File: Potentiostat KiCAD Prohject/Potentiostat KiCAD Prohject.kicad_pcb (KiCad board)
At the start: 2 copper layers, 94 x 55.9 mm, 35 parts, among them J1 USB_B_Micro, K1 DIPxx-1Axx-12xD, U1 OPA2277, U10 ADS1115IDGS, U11 MCP4725xxx-xCH, U12 RT9080-33GJ5, U2 TL074, U3 ESP32-S2, U4 OPA2277, U5 INA128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

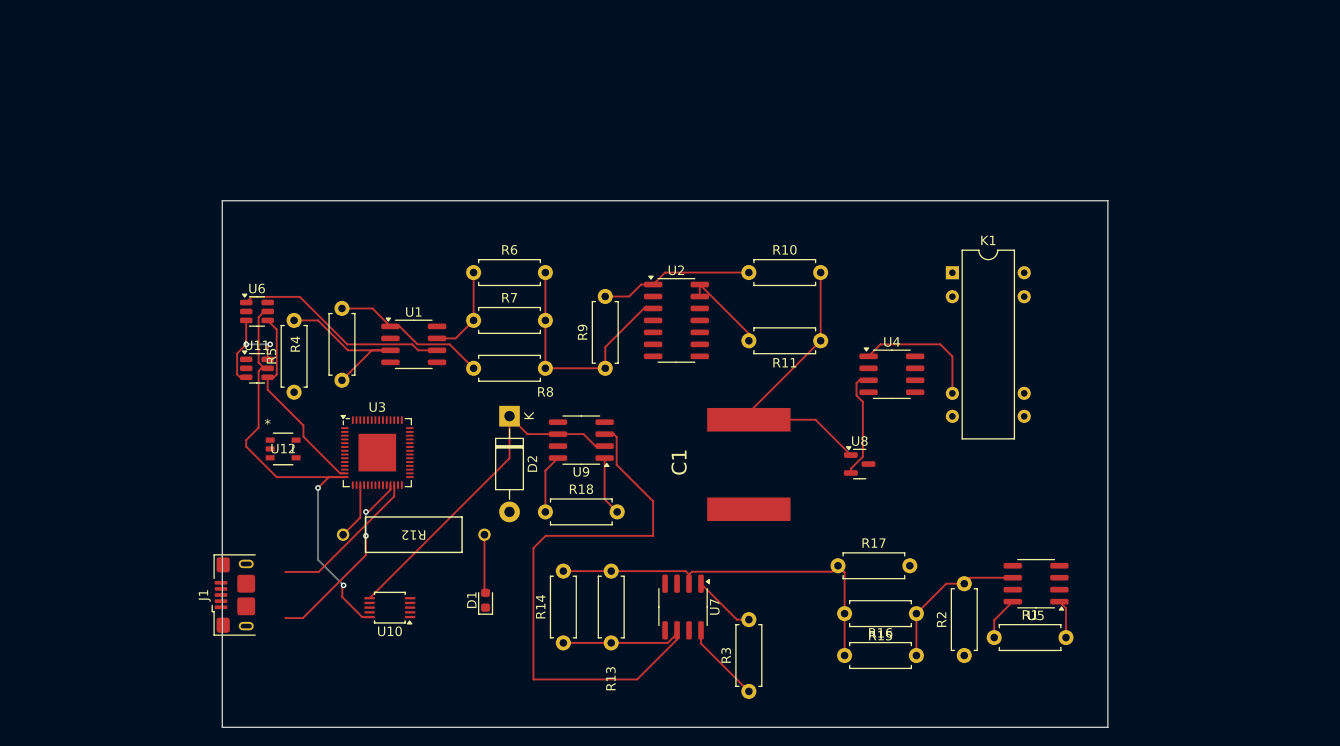
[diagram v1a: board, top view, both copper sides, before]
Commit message: Redid layout with ground traces
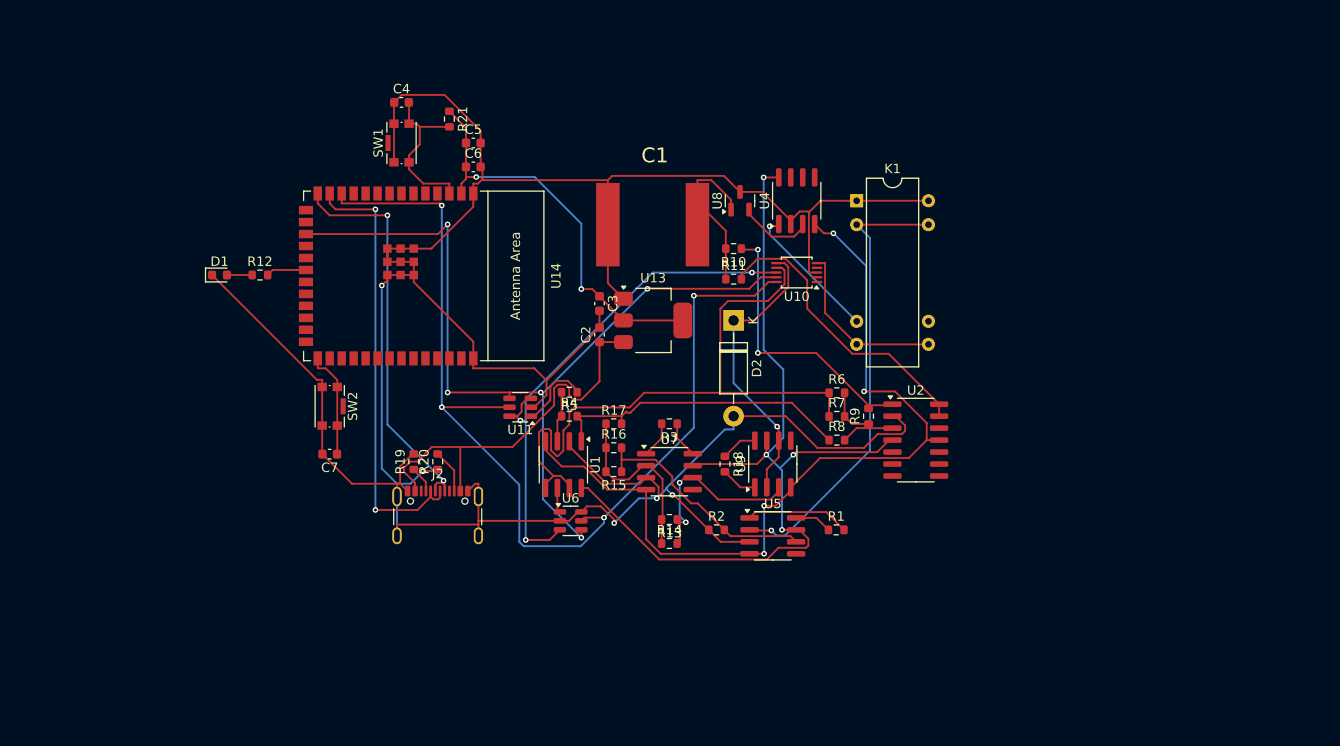
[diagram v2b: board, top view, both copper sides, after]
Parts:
- removed J1: USB_B_Micro, Connector_USB:USB_Micro-B_Amphenol_10118193-0001LF_Horizontal
- removed U12: RT9080-33GJ5, footprints:TSOT-23-5_RIT
- removed U3: ESP32-S2, Package_DFN_QFN:QFN-56-1EP_7x7mm_P0.4mm_EP4x4mm
- added C2: 100nF, Capacitor_SMD:C_0603_1608Metric, F.Cu at (172.1, 82.8)
- added C3: 10uF, Capacitor_SMD:C_0603_1608Metric, F.Cu at (172.1, 79.5)
- added C4: .1uF, Capacitor_SMD:C_0603_1608Metric, F.Cu at (151.1, 58.1)
- added C5: 1uF, Capacitor_SMD:C_0603_1608Metric, F.Cu at (158.7, 62.5)
- added C6: .1uF, Capacitor_SMD:C_0603_1608Metric, F.Cu at (158.7, 65.0)
- added C7: .1uF, Capacitor_SMD:C_0603_1608Metric, F.Cu at (143.5, 95.5)
- added J2: USB_C_Receptacle_USB2.0, Connector_USB:USB_C_Receptacle_GCT_USB4105-xx-A_16P_TopMnt_Horizontal, F.Cu at (154.9, 103.1)
- added R19: 5.1 k, Resistor_SMD:R_0603_1608Metric, F.Cu at (152.4, 96.3)
- added R20: 5.1 k, Resistor_SMD:R_0603_1608Metric, F.Cu at (154.9, 96.3)
- added R21: 10k, Resistor_SMD:R_0603_1608Metric, F.Cu at (156.2, 59.9)
- added SW1: Reset, Button_Switch_SMD:SW_Push_1P1T-SH_NO_CK_KMR2xxG, F.Cu at (151.1, 62.5)
- added SW2: Boot, Button_Switch_SMD:SW_Push_1P1T-SH_NO_CK_KMR2xxG, F.Cu at (143.5, 90.4)
- added U13: LD1117S33TR_SOT223, Package_TO_SOT_SMD:SOT-223-3_TabPin2, F.Cu at (177.8, 81.3)
- added U14: ESP32-S2-SOLO, ESP32:ESP32-S2-SOLO, F.Cu at (150.5, 76.6)
- R1, R10, R11, R13, R14, R15, R16, R17, R18, R2, R3, R4, R5, R6, R7, R8, R9: footprint Resistor_THT:R_Axial_DIN0207_L6.3mm_D2.5mm_P7.62mm_Horizontal -> Resistor_SMD:R_0603_1608Metric
- R12: footprint footprints:res2_1-1625885-7_TEC -> Resistor_SMD:R_0603_1608Metric
- moved U10 55.9 mm to (193.0, 76.2)
- moved D1 44.6 mm to (131.8, 76.5), turned to 0 degrees
- moved R6 40.6 mm to (197.3, 89.0)
- moved U6 40.0 mm to (169.0, 102.5)
- moved R7 39.9 mm to (197.3, 91.5)
- moved R8 39.3 mm to (197.3, 94.0)
- moved R12 36.4 mm to (136.1, 76.5), turned to 0 degrees
- moved R15 35.5 mm to (173.6, 97.3)
- moved R16 33.0 mm to (173.6, 94.8)
- moved U8 30.7 mm to (187.0, 68.6), turned to 90 degrees
- moved R3 29.6 mm to (179.5, 92.2), turned to 180 degrees
- moved R2 29.5 mm to (184.5, 103.5), turned to 0 degrees
- moved R5 29.2 mm to (168.9, 88.9), turned to 180 degrees
- moved U2 28.4 mm to (205.7, 94.0)
- moved R9 28.4 mm to (200.7, 91.4)
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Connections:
- net Net-(U10-AIN3) renamed /ADC_IN3
- net Net-(U10-SCL) renamed /I2C_SCL
- net Net-(U10-SDA) renamed /I2C_SDA
- R14 pad 1: Net-(U9-+) -> Net-(U7--)
- R14 pad 2: Net-(U7--) -> Net-(U9-+)
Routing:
- net GND: track 0.00 -> 323.6 mm, vias 0 -> 5
- net +9V: track 0.00 -> 96.0 mm, vias 0 -> 4
- net -9V: track 0.00 -> 89.1 mm, vias 0 -> 4
- net /I2C_SDA: track 21.1 -> 91.8 mm, vias 0 -> 5
- net /I2C_SCL: track 48.5 -> 108.2 mm, vias 2 -> 4
- net /ADC_IN3: track 9.74 -> 69.2 mm
- net Net-(U9-+): track 71.5 -> 20.4 mm, vias 0 -> 2
- net /Working Electrode: track 0.00 -> 48.9 mm, vias 0 -> 1
- net /D-: track 0.00 -> 47.0 mm, vias 0 -> 2
- net VCC: track 11.5 -> 55.9 mm, vias 2 -> 3
- net +3.3V: track 0.00 -> 43.0 mm, vias 0 -> 2
- net /D+: track 0.00 -> 42.4 mm, vias 0 -> 2
- net +5V: track 0.00 -> 41.7 mm
- net Net-(U2D--): track 9.40 -> 31.6 mm
- net Net-(U7--): track 40.5 -> 19.5 mm
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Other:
- board outline removed

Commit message: we're so back
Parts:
- added J1: Conn_01x02_Pin, Connector_PinHeader_2.54mm:PinHeader_1x02_P2.54mm_Vertical, F.Cu at (190.5, 61.0)
- added J3: Conn_01x02_Pin, Connector_PinHeader_2.54mm:PinHeader_1x02_P2.54mm_Vertical, F.Cu at (195.6, 58.4)
- added J4: Reference, i made this:CONN_575-8_KEY, F.Cu at (220.0, 65.3)
- added J5: Working, i made this:CONN_575-8_KEY, F.Cu at (220.0, 81.0)
- added J6: Working, i made this:CONN_575-8_KEY, F.Cu at (219.7, 97.5)
- U10: value ADS1115IDGS -> ADS1115
- U11: value MCP4725xxx-xCH -> MCP4725
- moved J2 2.54 mm to (154.9, 105.6)
- moved R19 2.54 mm to (152.4, 98.8)
- moved R20 2.54 mm to (154.9, 98.8)
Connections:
- K1 pad 13: /Working Electrode -> Net-(J5-Pin_1)
- K1 pad 2: /Working Electrode -> Net-(J5-Pin_1)
- U10 pad 1: unconnected-(U10-ADDR-Pad1) -> GND
- U2 pad 12: /Reference Electrode -> Net-(J4-Pin_1)
- U5 pad 2: /Working Electrode -> Net-(J6-Pin_1)
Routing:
- net GND: track 323.6 -> 25.0 mm, vias 5 -> 4
- net /Working Electrode: track 48.9 -> 0.00 mm, vias 1 -> 0
- net Net-(J6-Pin_1): track 0.00 -> 35.9 mm, vias 0 -> 2
- net Net-(J4-Pin_1): track 0.00 -> 33.1 mm, vias 0 -> 2
- net Net-(J5-Pin_1): track 0.00 -> 26.9 mm
- net -9V: track 89.1 -> 114.3 mm, vias 4 -> 5
- net /I2C_SCL: track 108.2 -> 92.4 mm, vias 4 -> 2
- net +3.3V: track 43.0 -> 58.8 mm
- net /D+: track 42.4 -> 52.3 mm
- net +9V: track 96.0 -> 101.2 mm, vias 4 -> 5
- net /I2C_SDA: track 91.8 -> 88.1 mm, vias 5 -> 3
- net Net-(R15-Pad1): track 25.2 -> 28.7 mm, vias 0 -> 2
- net /D-: track 47.0 -> 43.5 mm
- net Net-(R10-Pad1): track 29.7 -> 32.8 mm
- net Net-(J2-CC2): track 4.66 -> 7.51 mm, vias 0 -> 2
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- added copper zone on B.Cu, net GND
- added copper zone on F.Cu, net GND
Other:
- board outline added: 121.9 x 55.9 mm
- board text added: "/"

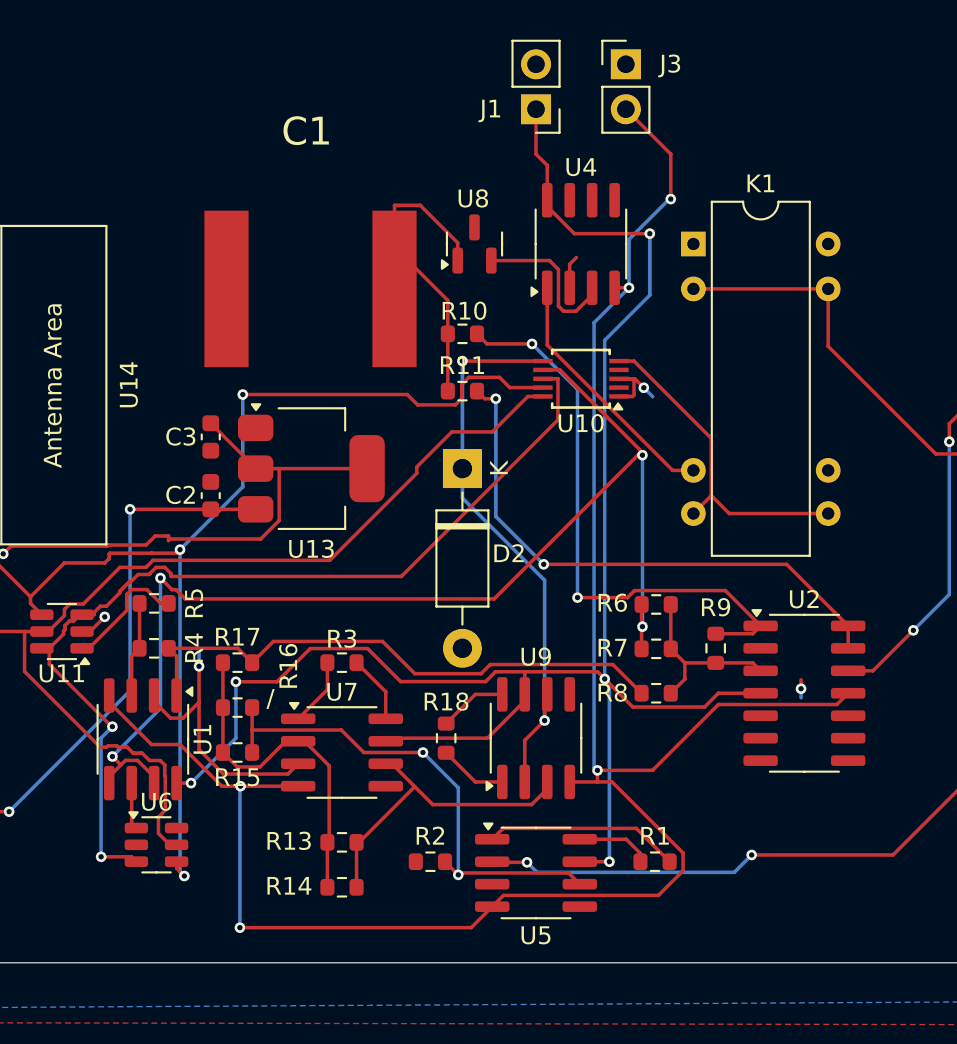
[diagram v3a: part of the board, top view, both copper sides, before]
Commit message: almost finished layout -- need test points
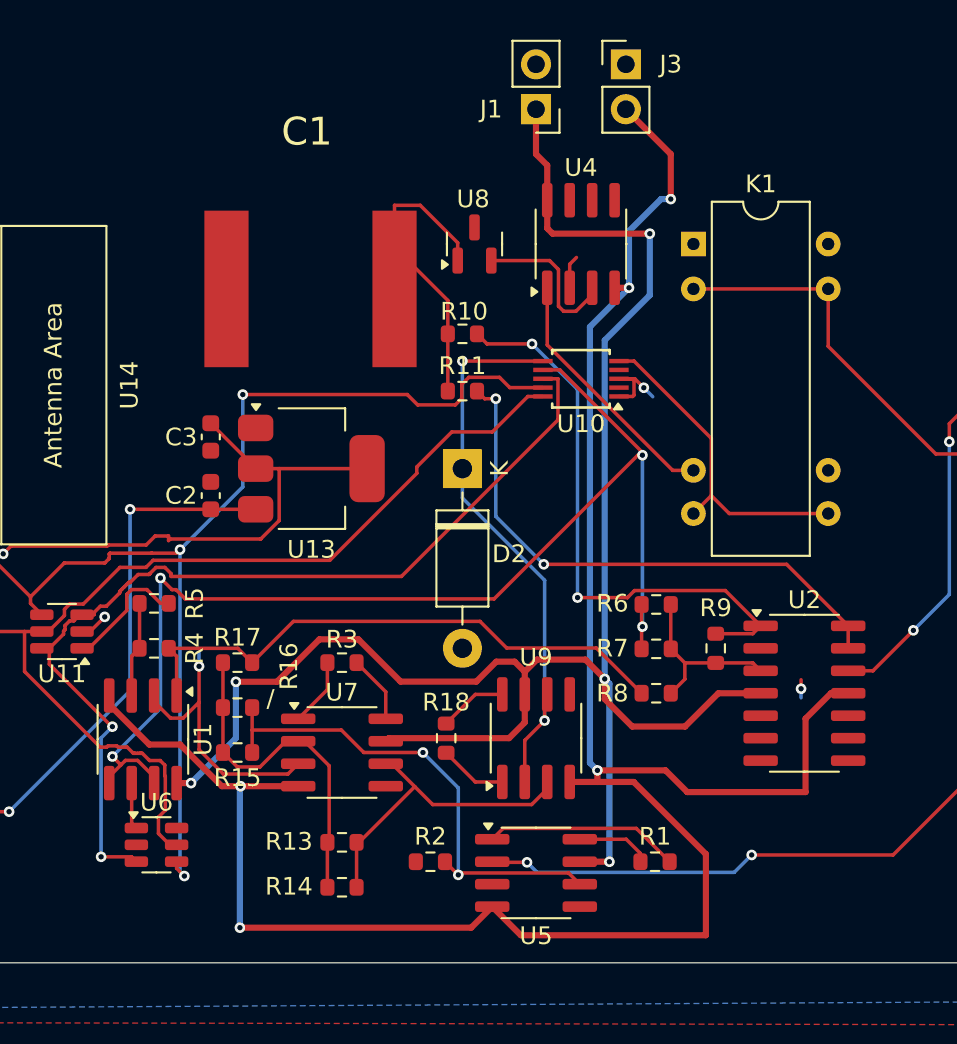
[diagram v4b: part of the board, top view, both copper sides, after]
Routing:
- net -9V: track 114.3 -> 124.3 mm
- net +9V: track 101.2 -> 105.7 mm
- net Net-(R17-Pad2): track 32.1 -> 32.6 mm

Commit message: finished!
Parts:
- added H1: MountingHole_Pad, MountingHole:MountingHole_2.2mm_M2_DIN965_Pad, F.Cu at (234.5, 57.5)
- added H2: MountingHole_Pad, MountingHole:MountingHole_2.2mm_M2_DIN965_Pad, F.Cu at (234.5, 105.5)
- added H3: MountingHole_Pad, MountingHole:MountingHole_2.2mm_M2_DIN965_Pad, F.Cu at (121.0, 105.5)
- added H4: MountingHole_Pad, MountingHole:MountingHole_2.2mm_M2_DIN965_Pad, F.Cu at (121.0, 57.5)
- added TP1: TestPoint, TestPoint:TestPoint_Pad_1.0x1.0mm, F.Cu at (212.9, 100.6)
- added TP10: TestPoint, TestPoint:TestPoint_Pad_1.0x1.0mm, F.Cu at (149.2, 87.9)
- added TP11: TestPoint, TestPoint:TestPoint_Pad_1.0x1.0mm, F.Cu at (155.5, 79.9)
- added TP12: TestPoint, TestPoint:TestPoint_Pad_1.0x1.0mm, F.Cu at (220.0, 71.5)
- added TP13: TestPoint, TestPoint:TestPoint_Pad_1.0x1.0mm, F.Cu at (211.5, 79.0)
- added TP14: TestPoint, TestPoint:TestPoint_Pad_1.0x1.0mm, F.Cu at (185.5, 64.5)
- added TP15: TestPoint, TestPoint:TestPoint_Pad_1.0x1.0mm, F.Cu at (188.0, 65.5)
- added TP16: TestPoint, TestPoint:TestPoint_Pad_1.0x1.0mm, F.Cu at (197.0, 78.5)
- added TP17: TestPoint, TestPoint:TestPoint_Pad_1.0x1.0mm, F.Cu at (200.5, 97.5)
- added TP18: TestPoint, TestPoint:TestPoint_Pad_1.0x1.0mm, F.Cu at (203.0, 88.0)
- added TP19: TestPoint, TestPoint:TestPoint_Pad_1.0x1.0mm, F.Cu at (166.0, 101.5)
- added TP2: TestPoint, TestPoint:TestPoint_Pad_1.0x1.0mm, F.Cu at (198.1, 64.0)
- added TP20: TestPoint, TestPoint:TestPoint_Pad_1.0x1.0mm, F.Cu at (164.0, 100.0)
- added TP21: TestPoint, TestPoint:TestPoint_Pad_1.0x1.0mm, F.Cu at (171.5, 90.0)
- added TP22: TestPoint, TestPoint:TestPoint_Pad_1.0x1.0mm, F.Cu at (173.5, 90.0)
- added TP23: TestPoint, TestPoint:TestPoint_Pad_1.0x1.0mm, F.Cu at (185.0, 106.0)
- added TP24: TestPoint, TestPoint:TestPoint_Pad_1.0x1.0mm, F.Cu at (176.5, 101.5)
- added TP25: TestPoint, TestPoint:TestPoint_Pad_1.0x1.0mm, F.Cu at (184.5, 100.0)
- added TP26: TestPoint, TestPoint:TestPoint_Pad_1.0x1.0mm, F.Cu at (194.5, 100.0)
- added TP3: TestPoint, TestPoint:TestPoint_Pad_1.0x1.0mm, F.Cu at (186.9, 58.4)
- added TP4: TestPoint, TestPoint:TestPoint_Pad_1.0x1.0mm, F.Cu at (187.5, 63.5)
- added TP5: TestPoint, TestPoint:TestPoint_Pad_1.0x1.0mm, F.Cu at (170.7, 107.2)
- added TP6: TestPoint, TestPoint:TestPoint_Pad_1.0x1.0mm, F.Cu at (166.6, 107.2)
- added TP7: TestPoint, TestPoint:TestPoint_Pad_1.0x1.0mm, F.Cu at (159.5, 93.0)
- added TP8: TestPoint, TestPoint:TestPoint_Pad_1.0x1.0mm, F.Cu at (164.6, 87.4)
- added TP9: TestPoint, TestPoint:TestPoint_Pad_1.0x1.0mm, F.Cu at (141.0, 101.0)
- J4: value Reference -> Reference Electrode
- J5, J6: value Working -> Working Electrode
- U10: value ADS1115 -> ADS1115IDGS
- U11: value MCP4725 -> MCP4725xxx-xCH
- moved C7 39.7 mm to (150.5, 56.4), turned to 0 degrees
- moved R21 37.0 mm to (137.8, 92.0), turned to 90 degrees
- moved C4 36.5 mm to (142.9, 93.7), turned to 180 degrees
- moved C5 35.8 mm to (135.2, 89.4), turned to 180 degrees
- moved C6 32.1 mm to (135.2, 86.9), turned to 180 degrees
- moved D1 30.4 mm to (162.2, 75.4), turned to 180 degrees
- moved SW2 29.7 mm to (150.5, 61.5), turned to 90 degrees
- moved SW1 28.2 mm to (142.9, 89.4), turned to -90 degrees
- moved R12 21.8 mm to (157.9, 75.4), turned to 180 degrees
- moved R19 10.9 mm to (144.0, 105.8), turned to -90 degrees
- moved R20 10.3 mm to (147.5, 106.0)
- moved U14 8.36 mm to (142.2, 75.0), turned to 90 degrees
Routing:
- net /D+: track 52.3 -> 22.8 mm, vias 2 -> 0
- net /D-: track 43.5 -> 23.4 mm, vias 2 -> 0
- net GND: track 25.0 -> 39.2 mm, vias 4 -> 224
- net +3.3V: track 58.8 -> 70.6 mm
- net Net-(J2-CC1): track 2.90 -> 12.6 mm, vias 0 -> 2
- net +5V: track 41.3 -> 50.0 mm
- net /I2C_SDA: track 88.1 -> 79.4 mm
- net Net-(D2-K): track 32.3 -> 39.6 mm
- net /I2C_SCL: track 92.4 -> 85.4 mm
- net Net-(J2-CC2): track 7.51 -> 12.7 mm
- net Net-(U2A-+): track 10.1 -> 15.1 mm, vias 0 -> 2
- net Net-(U4A-+): track 8.90 -> 13.7 mm
- net Net-(U14-EN): track 17.7 -> 22.0 mm
- net Net-(U8-IN): track 20.1 -> 23.2 mm
- net +9V: track 105.7 -> 108.7 mm
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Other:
- outline, holes or cut-outs redrawn
- board text added: "Benedict Cecilio, Sophie Sun, Yashil Trivedi"
- board text added: "HOPE"
- board text added: "Pocket Potentiostat"
- board text added: "堡垒之夜"
